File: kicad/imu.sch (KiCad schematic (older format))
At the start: 11 parts

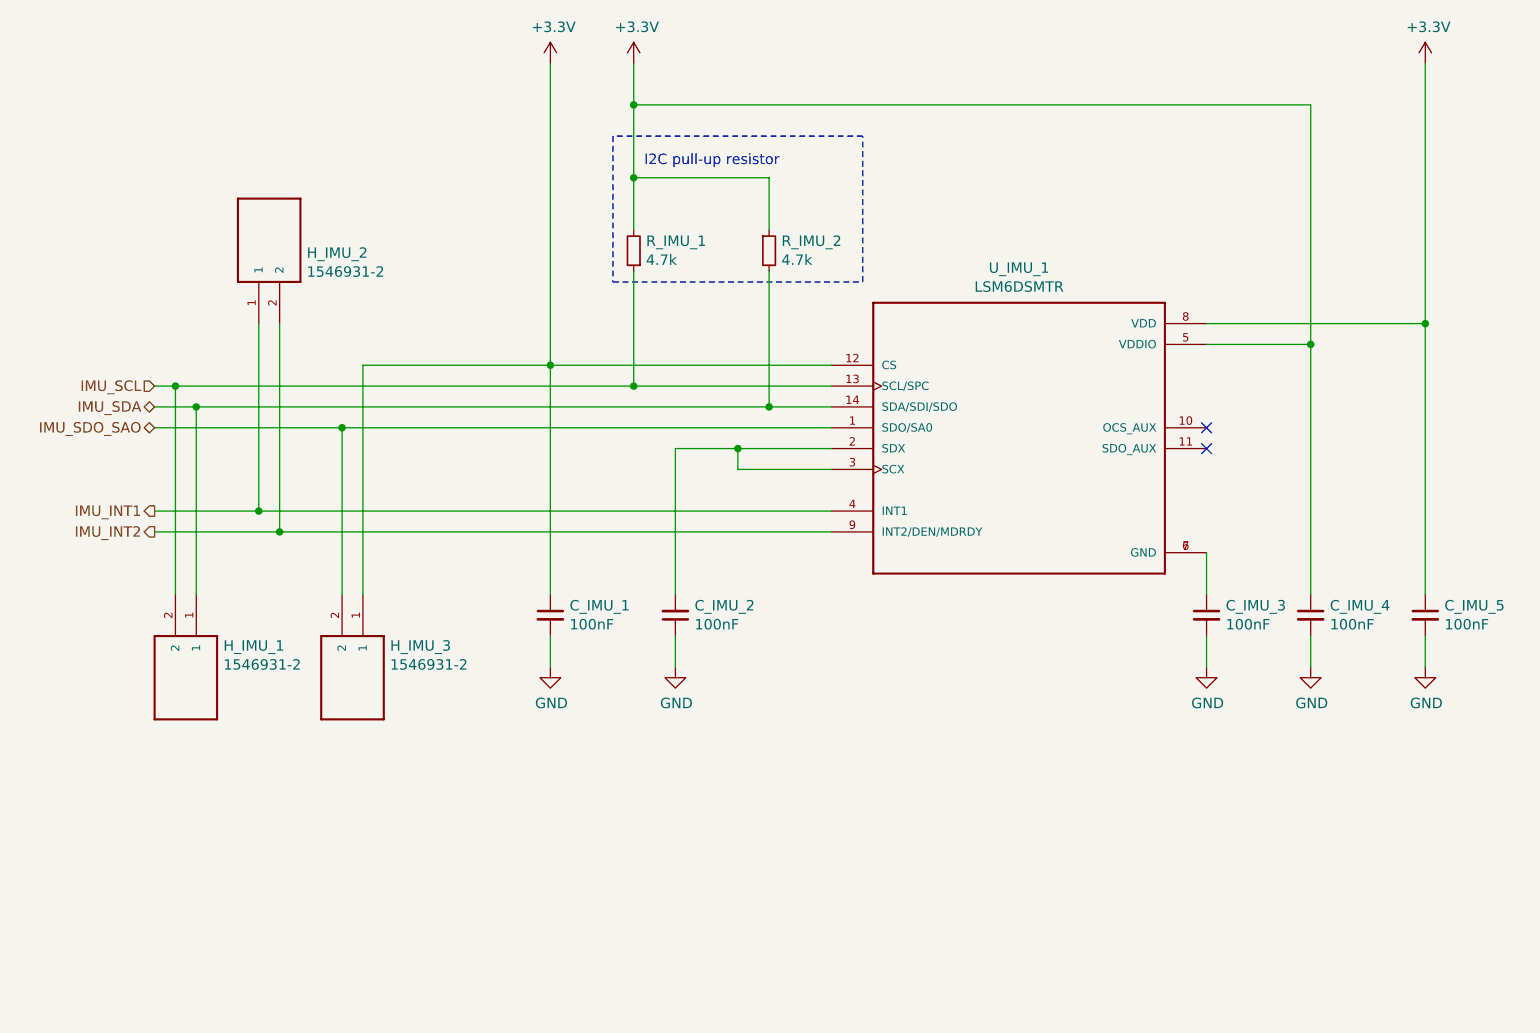
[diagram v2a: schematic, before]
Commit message: Updated schematic and PCB design to v0.0.2 for 2-layer pcb. Added more silkscreen text
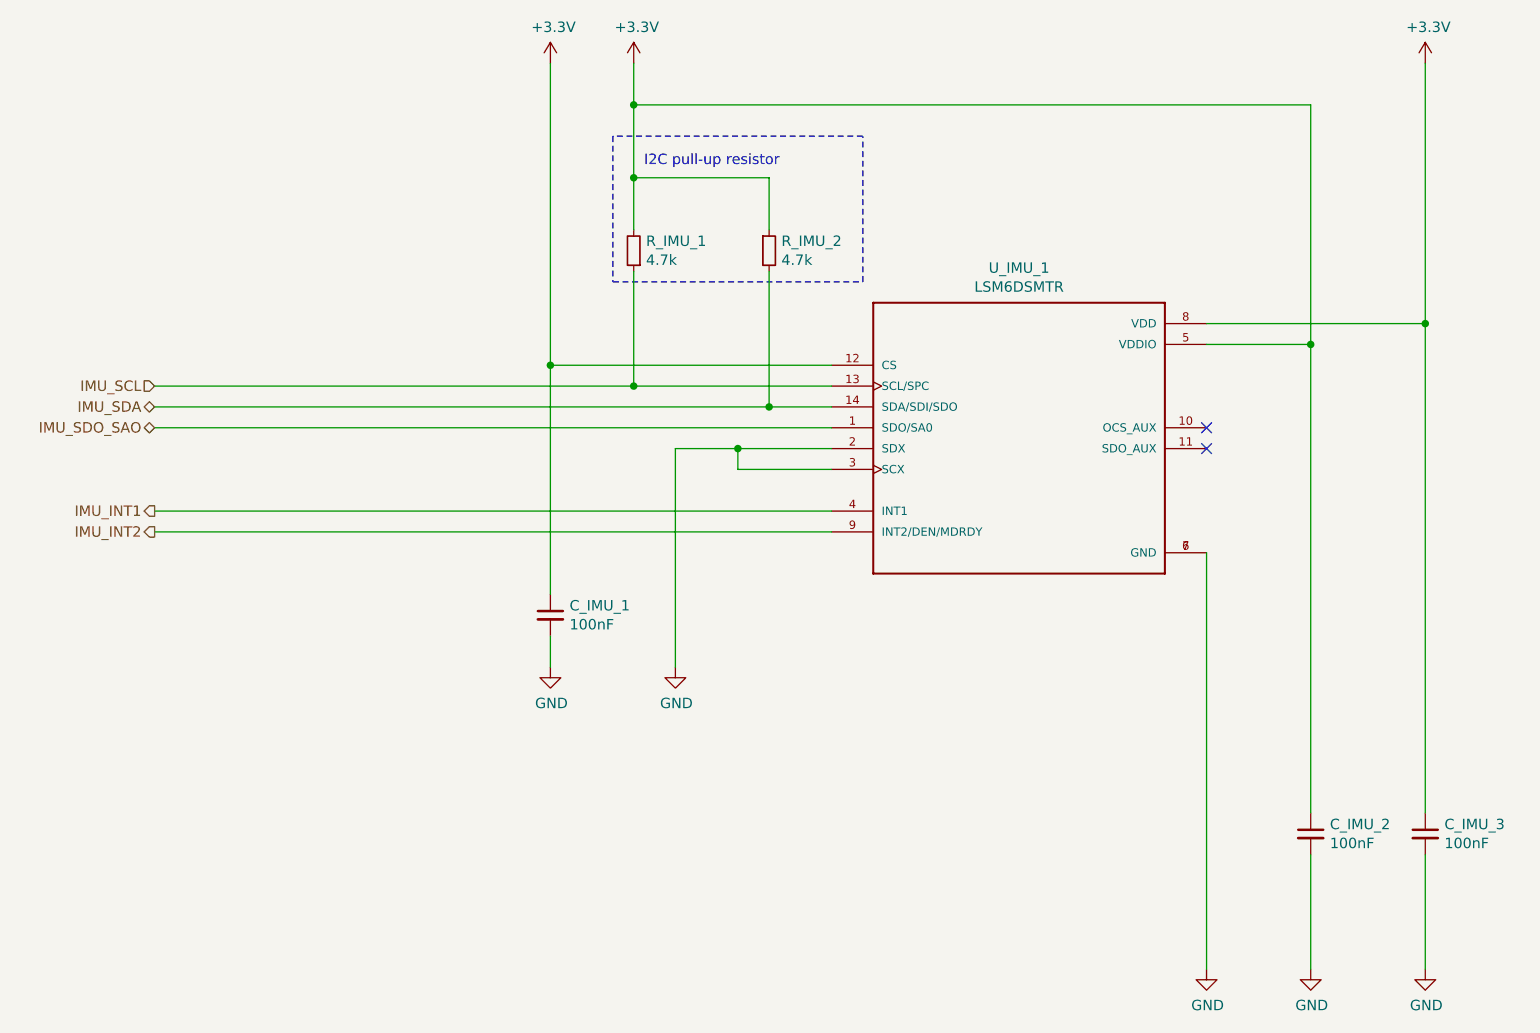
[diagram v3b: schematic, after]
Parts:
- removed C_IMU_2, C_IMU_3: 100nF, footprints:CAPC1608X90N, symbol Device:C_Small
- removed H_IMU_1, H_IMU_2, H_IMU_3: 1546931-2, footprints:1546931-2, symbol 1546931-2:1546931-2
- renumbered C_IMU_4 to C_IMU_2, C_IMU_5 to C_IMU_3
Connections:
- net GND: now also U_IMU_1.2 (SDX), U_IMU_1.3 (SCX), U_IMU_1.6 (GND), U_IMU_1.7 (GND)
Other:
- moved on the sheet: C_IMU_2, C_IMU_3
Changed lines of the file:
@@
 $Descr A4 11693 8268
 encoding utf-8
-Sheet 4 5
+Sheet 3 5
 Title "ESP32 Sensor Module | Inertia Measurement Unit"
-Date "2020-11-23"
-Rev "v0.0.1"
+Date "2020-11-24"
+Rev "v0.0.2"
 Comp "Created by Choong Jin Ng | jin3838@gmail.com"
 Comment1 ""
@@
 $EndDescr
 $Comp
-L Device:C_Small C_IMU_5
+L Device:C_Small C_IMU_3
 U 1 1 5FBCABEC
-P 8200 4300
-F 0 "C_IMU_5" H 8292 4346 50  0000 L CNN
-F 1 "100nF" H 8292 4255 50  0000 L CNN
-F 2 "footprints:CAPC1608X90N" H 8200 4300 50  0001 C CNN
-F 3 "https://product.tdk.com/info/en/catalog/datasheets/mlcc_commercial_midvoltage_en.pdf" H 8200 4300 50  0001 C CNN
-F 4 "TDK Corporation" H 8200 4300 50  0001 C CNN "Manufacturer"
-F 5 "C1608X7R2A103K080AA" H 8200 4300 50  0001 C CNN "Part Name"
-F 6 "DigiKey Canada" H 8200 4300 50  0001 C CNN "Vendor"
-F 7 "445-1304-1-ND" H 8200 4300 50  0001 C CNN "Vendor Part Name"
-	1    8200 4300
+P 8200 5350
+F 0 "C_IMU_3" H 8292 5396 50  0000 L CNN
+F 1 "100nF" H 8292 5305 50  0000 L CNN
+F 2 "footprints:CAPC1608X90N" H 8200 5350 50  0001 C CNN
+F 3 "https://product.tdk.com/info/en/catalog/datasheets/mlcc_commercial_midvoltage_en.pdf" H 8200 5350 50  0001 C CNN
+F 4 "TDK Corporation" H 8200 5350 50  0001 C CNN "Manufacturer"
+F 5 "C1608X7R2A103K080AA" H 8200 5350 50  0001 C CNN "Part Name"
+F 6 "DigiKey Canada" H 8200 5350 50  0001 C CNN "Vendor"
+F 7 "445-1304-1-ND" H 8200 5350 50  0001 C CNN "Vendor Part Name"
+	1    8200 5350
 	1    0    0    -1
 $EndComp
@@
 L power:GND #PWR0125
 U 1 1 5FBCDDD5
-P 8200 4550
-F 0 "#PWR0125" H 8200 4300 50  0001 C CNN
-F 1 "GND" H 8205 4377 50  0000 C CNN
-F 2 "" H 8200 4550 50  0001 C CNN
-F 3 "" H 8200 4550 50  0001 C CNN
-	1    8200 4550
+P 8200 6000
+F 0 "#PWR0125" H 8200 5750 50  0001 C CNN
+F 1 "GND" H 8205 5827 50  0000 C CNN
+F 2 "" H 8200 6000 50  0001 C CNN
+F 3 "" H 8200 6000 50  0001 C CNN
+	1    8200 6000
 	1    0    0    -1
 $EndComp
@@
 NoConn ~ 7150 3400
 NoConn ~ 7150 3500
-Text HLabel 2100 3400 0    50   BiDi ~ 0
-IMU_SDO_SAO
 $Comp
 L Device:R_Small R_IMU_1
@@
 $EndComp
 Wire Wire Line
-	8200 4550 8200 4400
-Wire Wire Line
-	7650 4550 7650 4400
-Wire Wire Line
 	4400 2650 4400 3200
 Connection ~ 4400 3200
@@
 	5050 2650 5050 3300
 Connection ~ 5050 3300
-Wire Wire Line
-	7650 3000 7650 4200
-Wire Wire Line
-	8200 2900 8200 4200
 Connection ~ 8200 2900
-Wire Wire Line
-	2100 3300 2300 3300
-Wire Wire Line
-	2100 3200 2200 3200
 Wire Wire Line
 	5050 2450 5050 2200
@@
 Connection ~ 4000 3100
 $Comp
-L Device:C_Small C_IMU_4
+L Device:C_Small C_IMU_2
 U 1 1 5FBF7A62
-P 7650 4300
-F 0 "C_IMU_4" H 7742 4346 50  0000 L CNN
-F 1 "100nF" H 7742 4255 50  0000 L CNN
-F 2 "footprints:CAPC1608X90N" H 7650 4300 50  0001 C CNN
-F 3 "https://product.tdk.com/info/en/catalog/datasheets/mlcc_commercial_midvoltage_en.pdf" H 7650 4300 50  0001 C CNN
-F 4 "TDK Corporation" H 7650 4300 50  0001 C CNN "Manufacturer"
-F 5 "C1608X7R2A103K080AA" H 7650 4300 50  0001 C CNN "Part Name"
-F 6 "DigiKey Canada" H 7650 4300 50  0001 C CNN "Vendor"
-F 7 "445-1304-1-ND" H 7650 4300 50  0001 C CNN "Vendor Part Name"
-	1    7650 4300
+P 7650 5350
+F 0 "C_IMU_2" H 7742 5396 50  0000 L CNN
+F 1 "100nF" H 7742 5305 50  0000 L CNN
+F 2 "footprints:CAPC1608X90N" H 7650 5350 50  0001 C CNN
+F 3 "https://product.tdk.com/info/en/catalog/datasheets/mlcc_commercial_midvoltage_en.pdf" H 7650 5350 50  0001 C CNN
+F 4 "TDK Corporation" H 7650 5350 50  0001 C CNN "Manufacturer"
+F 5 "C1608X7R2A103K080AA" H 7650 5350 50  0001 C CNN "Part Name"
+F 6 "DigiKey Canada" H 7650 5350 50  0001 C CNN "Vendor"
+F 7 "445-1304-1-ND" H 7650 5350 50  0001 C CNN "Vendor Part Name"
+	1    7650 5350
 	1    0    0    -1
 $EndComp
@@
 L power:GND #PWR0130
 U 1 1 5FBF7FC2
-P 7650 4550
-F 0 "#PWR0130" H 7650 4300 50  0001 C CNN
-F 1 "GND" H 7655 4377 50  0000 C CNN
-F 2 "" H 7650 4550 50  0001 C CNN
-F 3 "" H 7650 4550 50  0001 C CNN
-	1    7650 4550
+P 7650 6000
+F 0 "#PWR0130" H 7650 5750 50  0001 C CNN
+F 1 "GND" H 7655 5827 50  0000 C CNN
+F 2 "" H 7650 6000 50  0001 C CNN
+F 3 "" H 7650 6000 50  0001 C CNN
+	1    7650 6000
 	1    0    0    -1
 $EndComp
@@
 Wire Wire Line
 	5350 3100 4000 3100
-Wire Wire Line
-	2100 3400 3000 3400
 $Comp
 L LSM6DSMTR:LSM6DSMTR U_IMU_1
@@
 L power:GND #PWR0131
 U 1 1 5FBD62BA
-P 7150 4550
-F 0 "#PWR0131" H 7150 4300 50  0001 C CNN
-F 1 "GND" H 7155 4377 50  0000 C CNN
-F 2 "" H 7150 4550 50  0001 C CNN
-F 3 "" H 7150 4550 50  0001 C CNN
-	1    7150 4550
-	1    0    0    -1
-$EndComp
-$Comp
-L Device:C_Small C_IMU_3
-U 1 1 5FBFE448
-P 7150 4300
-F 0 "C_IMU_3" H 7242 4346 50  0000 L CNN
-F 1 "100nF" H 7242 4255 50  0000 L CNN
-F 2 "footprints:CAPC1608X90N" H 7150 4300 50  0001 C CNN
-F 3 "https://product.tdk.com/info/en/catalog/datasheets/mlcc_commercial_midvoltage_en.pdf" H 7150 4300 50  0001 C CNN
-F 4 "TDK Corporation" H 7150 4300 50  0001 C CNN "Manufacturer"
-F 5 "C1608X7R2A103K080AA" H 7150 4300 50  0001 C CNN "Part Name"
-F 6 "DigiKey Canada" H 7150 4300 50  0001 C CNN "Vendor"
-F 7 "445-1304-1-ND" H 7150 4300 50  0001 C CNN "Vendor Part Name"
-	1    7150 4300
-	1    0    0    -1
-$EndComp
-Wire Wire Line
-	7150 4000 7150 4200
-Wire Wire Line
-	7150 4400 7150 4550
+P 7150 6000
+F 0 "#PWR0131" H 7150 5750 50  0001 C CNN
+F 1 "GND" H 7155 5827 50  0000 C CNN
+F 2 "" H 7150 6000 50  0001 C CNN
+F 3 "" H 7150 6000 50  0001 C CNN
+	1    7150 6000
+	1    0    0    -1
+$EndComp
 Wire Wire Line
 	7150 2900 8200 2900
 Wire Wire Line
 	7150 3000 7650 3000
-$Comp
-L Device:C_Small C_IMU_2
-U 1 1 5FC045BE
-P 4600 4300
-F 0 "C_IMU_2" H 4508 4254 50  0000 R CNN
-F 1 "100nF" H 4508 4345 50  0000 R CNN
-F 2 "footprints:CAPC1608X90N" H 4600 4300 50  0001 C CNN
-F 3 "https://product.tdk.com/info/en/catalog/datasheets/mlcc_commercial_midvoltage_en.pdf" H 4600 4300 50  0001 C CNN
-F 4 "TDK Corporation" H 4600 4300 50  0001 C CNN "Manufacturer"
-F 5 "C1608X7R2A103K080AA" H 4600 4300 50  0001 C CNN "Part Name"
-F 6 "DigiKey Canada" H 4600 4300 50  0001 C CNN "Vendor"
-F 7 "445-1304-1-ND" H 4600 4300 50  0001 C CNN "Vendor Part Name"
-	1    4600 4300
-	-1   0    0    1
-$EndComp
-Wire Wire Line
-	4600 4550 4600 4400
-Wire Wire Line
-	4600 3500 4600 4200
 Wire Wire Line
 	4600 3500 4900 3500
@@
 $EndComp
 Wire Wire Line
-	8200 1650 8200 2900
-Wire Wire Line
 	4400 1650 4400 1850
 Wire Wire Line
 	4400 1850 7650 1850
-Wire Wire Line
-	7650 1850 7650 3000
 Connection ~ 4400 1850
 Wire Wire Line
 	4400 1850 4400 2200
 Connection ~ 7650 3000
-Wire Wire Line
-	2100 3800 2600 3800
 Text HLabel 2100 3800 0    50   Output ~ 0
 IMU_INT1
@@
 IMU_INT2
 Wire Wire Line
-	2200 4200 2200 3200
-Connection ~ 2200 3200
-Wire Wire Line
-	2200 3200 4400 3200
-Wire Wire Line
-	2300 4200 2300 3300
-Connection ~ 2300 3300
-Wire Wire Line
-	2300 3300 5050 3300
-Wire Wire Line
-	3000 4200 3000 3400
-Connection ~ 3000 3400
-Wire Wire Line
-	3000 3400 5350 3400
-Wire Wire Line
-	3100 4200 3100 3100
-Wire Wire Line
-	3100 3100 4000 3100
-$Comp
-L 1546931-2:1546931-2 H_IMU_2
-U 1 1 5FD97AB3
-P 2700 2500
-F 0 "H_IMU_2" V 2639 2370 50  0000 R CNN
-F 1 "1546931-2" V 2548 2370 50  0000 R CNN
-F 2 "footprints:1546931-2" H 2700 2500 50  0001 L BNN
-F 3 "https://www.te.com/commerce/DocumentDelivery/DDEController?Action=srchrtrv&DocNm=1-1773458-1_EURO_STYLE_QRG&DocType=DS&DocLang=English" H 2700 2500 50  0001 L BNN
-F 4 "1546931-2" H 2700 2500 50  0001 C CNN "Part Name"
-F 5 "TE Connectivity AMP Connectors" H 2700 2500 50  0001 C CNN "Manufacturer"
-F 6 "Digikey Canada" H 2700 2500 50  0001 C CNN "Vendor"
-F 7 "" H 2700 2500 50  0001 C CNN "digikeypn"
-F 8 "A97965-ND" H 2700 2500 50  0001 C CNN "Vendor Part Name"
-	1    2700 2500
-	0    -1   -1   0
-$EndComp
-Wire Wire Line
-	2600 2900 2600 3800
-Connection ~ 2600 3800
-Wire Wire Line
-	2600 3800 5350 3800
-Wire Wire Line
-	2700 2900 2700 3900
-Wire Wire Line
-	2100 3900 2700 3900
-Connection ~ 2700 3900
-Wire Wire Line
-	2700 3900 5350 3900
-$Comp
-L 1546931-2:1546931-2 H_IMU_3
-U 1 1 5FD94A28
-P 3000 4600
-F 0 "H_IMU_3" V 2847 4830 50  0000 L CNN
-F 1 "1546931-2" V 2938 4830 50  0000 L CNN
-F 2 "footprints:1546931-2" H 3000 4600 50  0001 L BNN
-F 3 "https://www.te.com/commerce/DocumentDelivery/DDEController?Action=srchrtrv&DocNm=1-1773458-1_EURO_STYLE_QRG&DocType=DS&DocLang=English" H 3000 4600 50  0001 L BNN
-F 4 "1546931-2" H 3000 4600 50  0001 C CNN "Part Name"
-F 5 "TE Connectivity AMP Connectors" H 3000 4600 50  0001 C CNN "Manufacturer"
-F 6 "Digikey Canada" H 3000 4600 50  0001 C CNN "Vendor"
-F 7 "" H 3000 4600 50  0001 C CNN "digikeypn"
-F 8 "A97965-ND" H 3000 4600 50  0001 C CNN "Vendor Part Name"
-	1    3000 4600
-	0    1    1    0
-$EndComp
-$Comp
-L 1546931-2:1546931-2 H_IMU_1
-U 1 1 5FD93D24
-P 2200 4600
-F 0 "H_IMU_1" V 2047 4830 50  0000 L CNN
-F 1 "1546931-2" V 2138 4830 50  0000 L CNN
-F 2 "footprints:1546931-2" H 2200 4600 50  0001 L BNN
-F 3 "https://www.te.com/commerce/DocumentDelivery/DDEController?Action=srchrtrv&DocNm=1-1773458-1_EURO_STYLE_QRG&DocType=DS&DocLang=English" H 2200 4600 50  0001 L BNN
-F 4 "1546931-2" H 2200 4600 50  0001 C CNN "Part Name"
-F 5 "TE Connectivity AMP Connectors" H 2200 4600 50  0001 C CNN "Manufacturer"
-F 6 "Digikey Canada" H 2200 4600 50  0001 C CNN "Vendor"
-F 7 "" H 2200 4600 50  0001 C CNN "digikeypn"
-F 8 "A97965-ND" H 2200 4600 50  0001 C CNN "Vendor Part Name"
-	1    2200 4600
-	0    1    1    0
-$EndComp
+	8200 1650 8200 2900
+Wire Wire Line
+	7650 1850 7650 3000
+Wire Wire Line
+	7650 5450 7650 6000
+Wire Wire Line
+	8200 5450 8200 6000
+Wire Wire Line
+	8200 2900 8200 5250
+Wire Wire Line
+	7650 3000 7650 5250
+Wire Wire Line
+	2100 3200 4400 3200
+Wire Wire Line
+	2100 3300 5050 3300
+Wire Wire Line
+	2100 3800 5350 3800
+Wire Wire Line
+	2100 3900 5350 3900
+Wire Wire Line
+	2100 3400 5350 3400
+Text HLabel 2100 3400 0    50   BiDi ~ 0
+IMU_SDO_SAO
+Wire Wire Line
+	7150 4000 7150 6000
+Wire Wire Line
+	4600 3500 4600 4550
 $EndSCHEMATC
